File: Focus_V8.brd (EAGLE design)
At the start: 64.8 x 96.5 mm, 104 parts

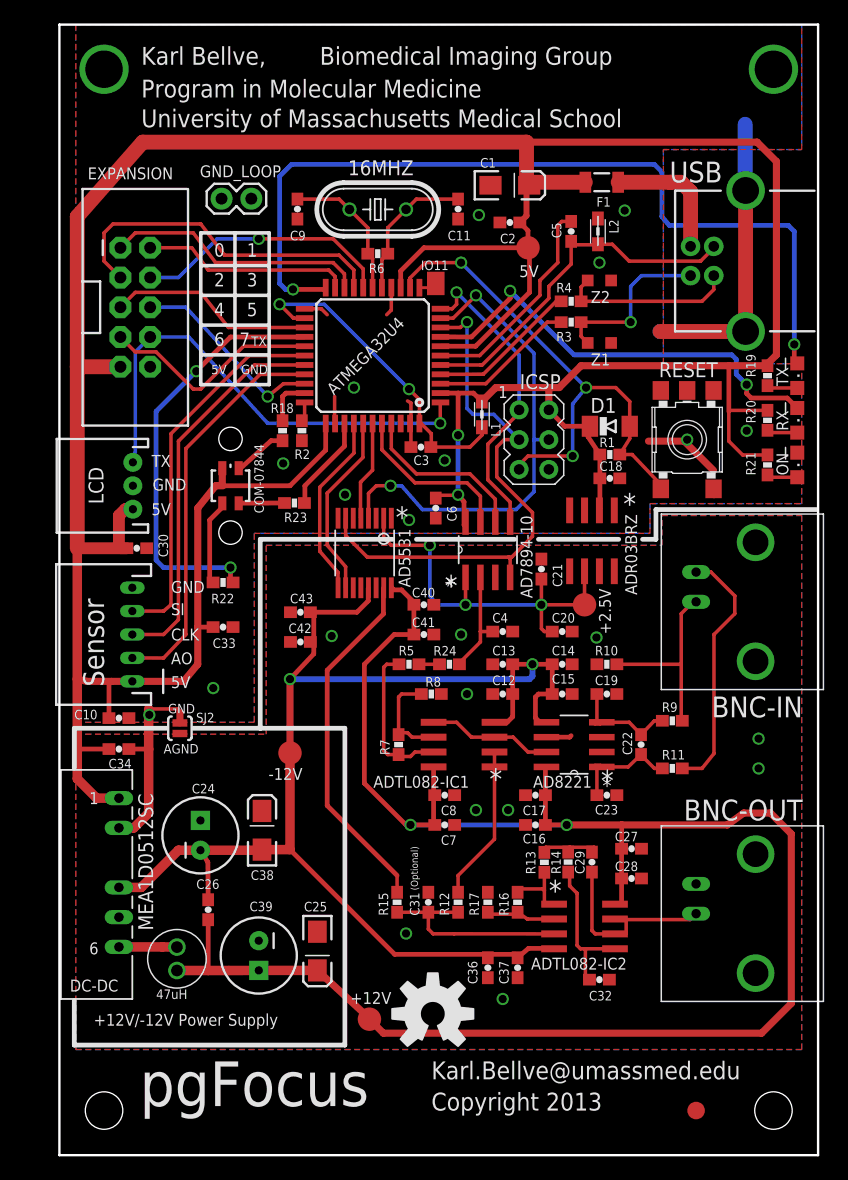
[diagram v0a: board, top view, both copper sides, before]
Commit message: Change connection between analog and digital ground plans via a cutable trace, which means that both ground planes will be connected by default.
Also pin 6 (RBEN) of AD5531 was mistakenly left floating, now connected to 5V line to
force deactivation.
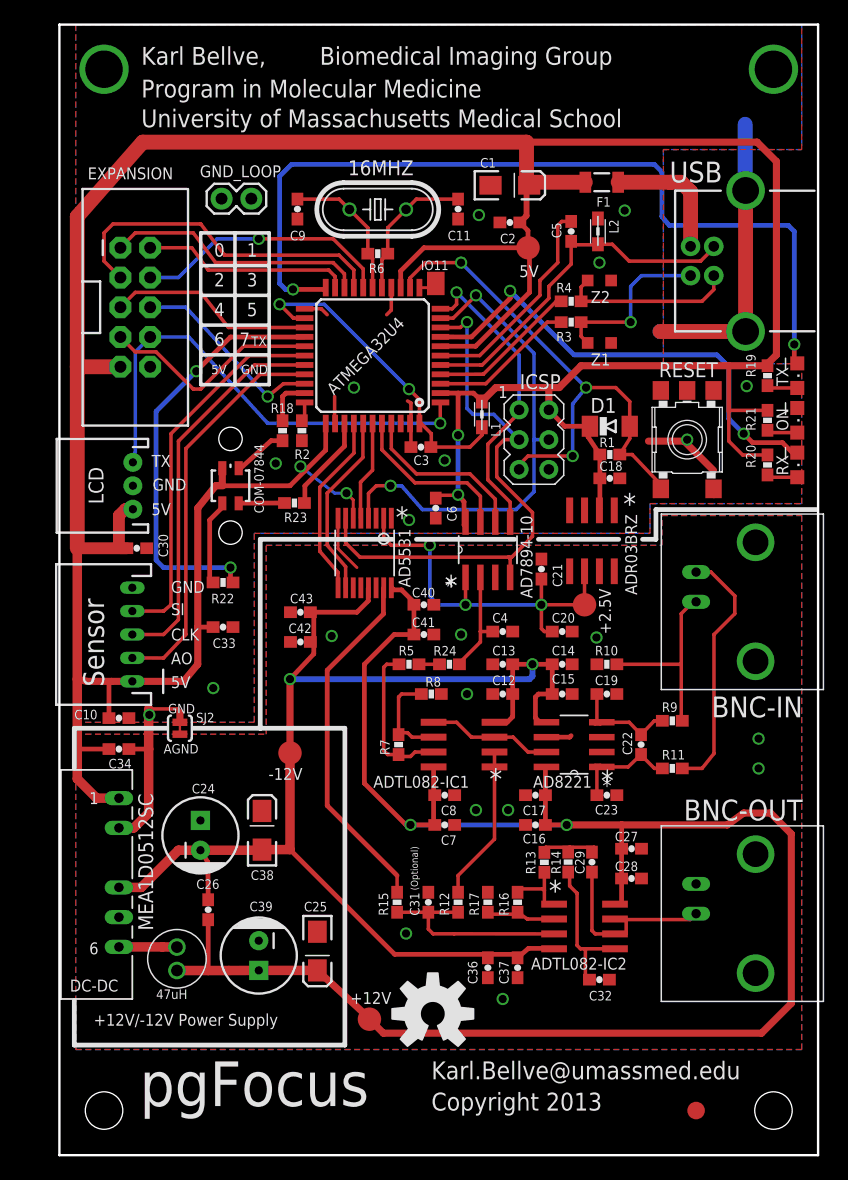
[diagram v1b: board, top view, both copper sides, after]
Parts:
- C21, C30: value 1uF -> 1uF (16V)
- F1: value MF-NSMF050-2 -> MF-MSMF050-2
- R10: value 1M -> 100k
- SJ2: value SOLDERJUMPERNO -> SOLDERJUMPERTRACE; device SparkFun-Passives:SJ_2S-NO -> SparkFun-Passives:SJ_2S-TRACE
- U$1: value AD5331 -> AD5531
- moved ON 3.81 mm to (98.6, 60.2)
- moved R20 3.81 mm to (96.0, 56.4)
- moved R21 3.81 mm to (96.0, 60.2)
- moved RX 3.81 mm to (98.6, 56.4)
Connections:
- net +5V: now also U$1.RBEN
- net AGND: now also U$1.SDO
- net GND: no longer U$1.SDO
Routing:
- net +5V: track 307.5 -> 315.3 mm, vias 2 -> 4
- net AGND: track 2.16 -> 7.04 mm
- net RXLED: track 37.8 -> 40.8 mm
- net GND: vias 14 -> 13
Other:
- board text added: "PMM"
- board text removed: "Collaborators"

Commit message: Updating to eliminate serial LCD connector, and to make a horizontal expansion possible. This simplifies using a box to contain the PCB
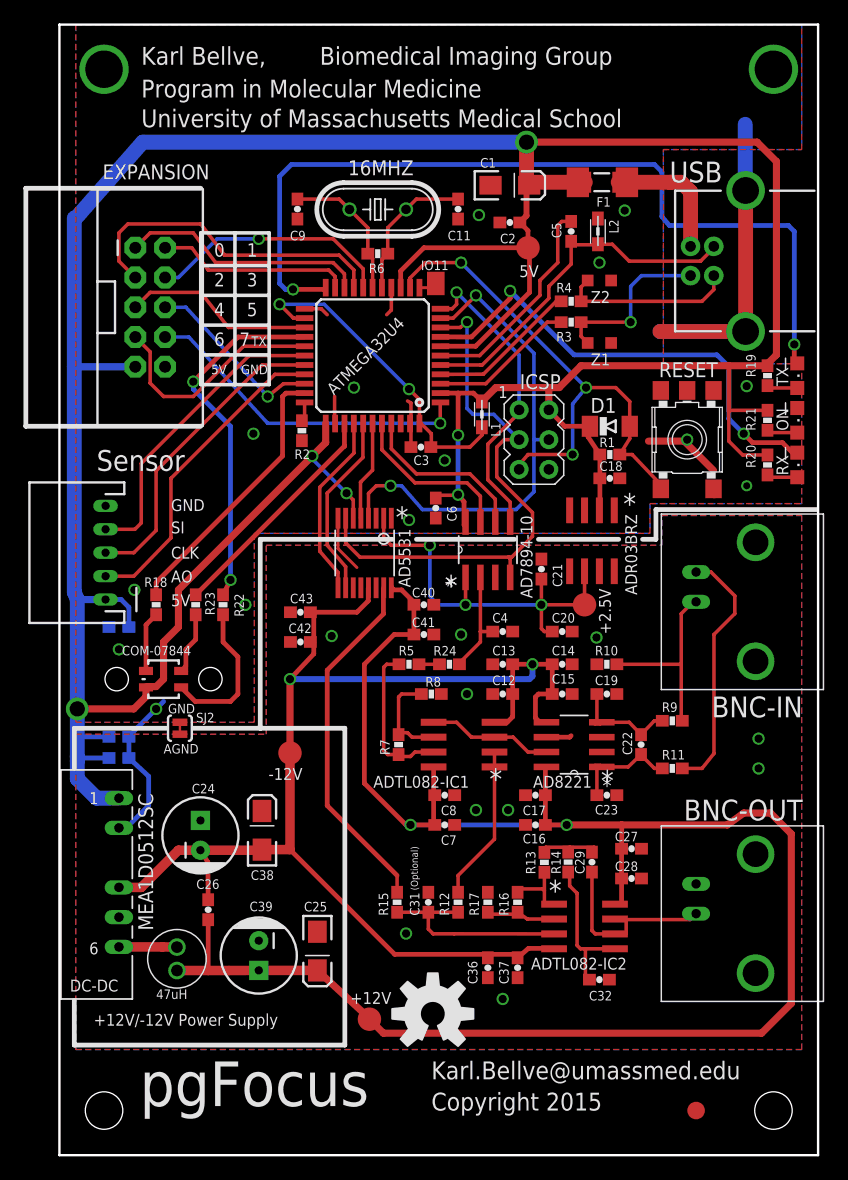
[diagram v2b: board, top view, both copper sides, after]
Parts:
- removed C30: 1uF (16V), SparkFun:0603-CAP
- removed GND_LOOP: 0, SparkFun:1X02
- removed LCD: LCD-09394, SparkFun-Connectors:JST-3-PTH
- C11, C9: value 18pF (16V) -> 22pF (16V)
- F1: value MF-MSMF050-2 -> MF-NSMF050-2
- R7, R8: value 10K -> 10K 0.1%
- moved R18 18.4 mm to (43.8, 44.5)
- moved COM-07844 17.5 mm to (44.5, 38.1), turned to 270 degrees
- moved U$2 17.5 mm to (44.5, 38.1), turned to 90 degrees
- moved R23 12.1 mm to (47.2, 44.5), turned to 270 degrees
- moved C33 8.89 mm to (40.6, 42.5), flipped to the bottom
- moved SENSOR 7.35 mm to (39.5, 48.9)
- moved R22 1.90 mm to (49.5, 44.5), turned to 270 degrees
- moved C10 1.60 mm to (40.6, 33.2), flipped to the bottom, turned to 180 degrees
- moved EXPANSION 1.27 mm to (43.3, 69.8)
- moved C34 0.76 mm to (40.6, 31.4), flipped to the bottom, turned to 180 degrees
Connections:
- net +5V: no longer C30.1, LCD.1
- net D7: no longer LCD.3
- net GND: now also RESET.4, RESET.5; no longer C30.2, GND_LOOP.1, GND_LOOP.2, LCD.2
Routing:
- net IO13: track 4.08 -> 23.4 mm
- net D7: track 41.1 -> 28.5 mm
- net A0: track 8.20 -> 19.9 mm
- net TSL1401R_AO: track 34.1 -> 27.1 mm
- net TSL1401R_CLK: track 33.2 -> 26.6 mm
- net +5V: track 315.3 -> 309.0 mm, vias 4 -> 6
- net TSL1401R_SI: track 32.3 -> 26.1 mm
- net N$30: track 7.32 -> 12.9 mm
- net IO12: track 35.9 -> 30.8 mm
- net GND: track 68.9 -> 65.7 mm, vias 13 -> 16
- net N$31: track 3.92 -> 5.75 mm
- net D2/SDA: track 29.4 -> 28.1 mm
- net D0/RX: track 22.5 -> 21.2 mm
- net D5: track 16.9 -> 15.7 mm
- net D4: track 17.8 -> 16.5 mm
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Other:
- board text added: "Copyright 2015"
- board text added: "June 25 2015"
- board text added: "Molecular Medicine"
- board text removed: "April 30, 2013"
- board text removed: "Clive Standley"
- board text removed: "PMM"
